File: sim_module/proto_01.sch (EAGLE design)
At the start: 4 parts, among them IC1 SIM900

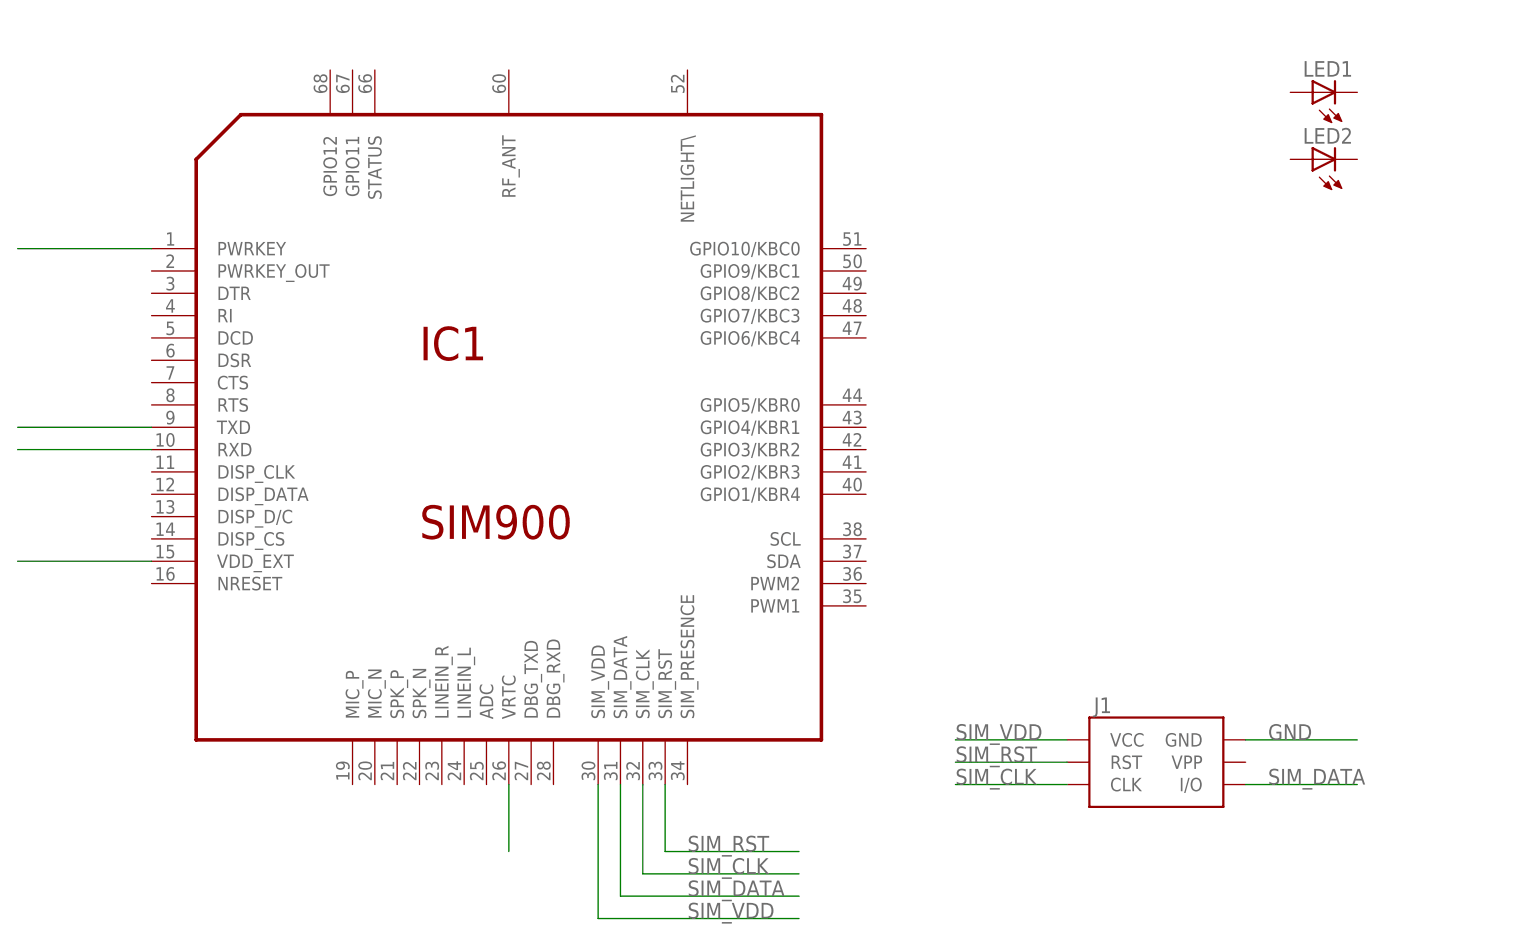
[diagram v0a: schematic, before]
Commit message: Connected leds to status and netlight pins in schematics
Connected leds to status and netlight pins in schematics
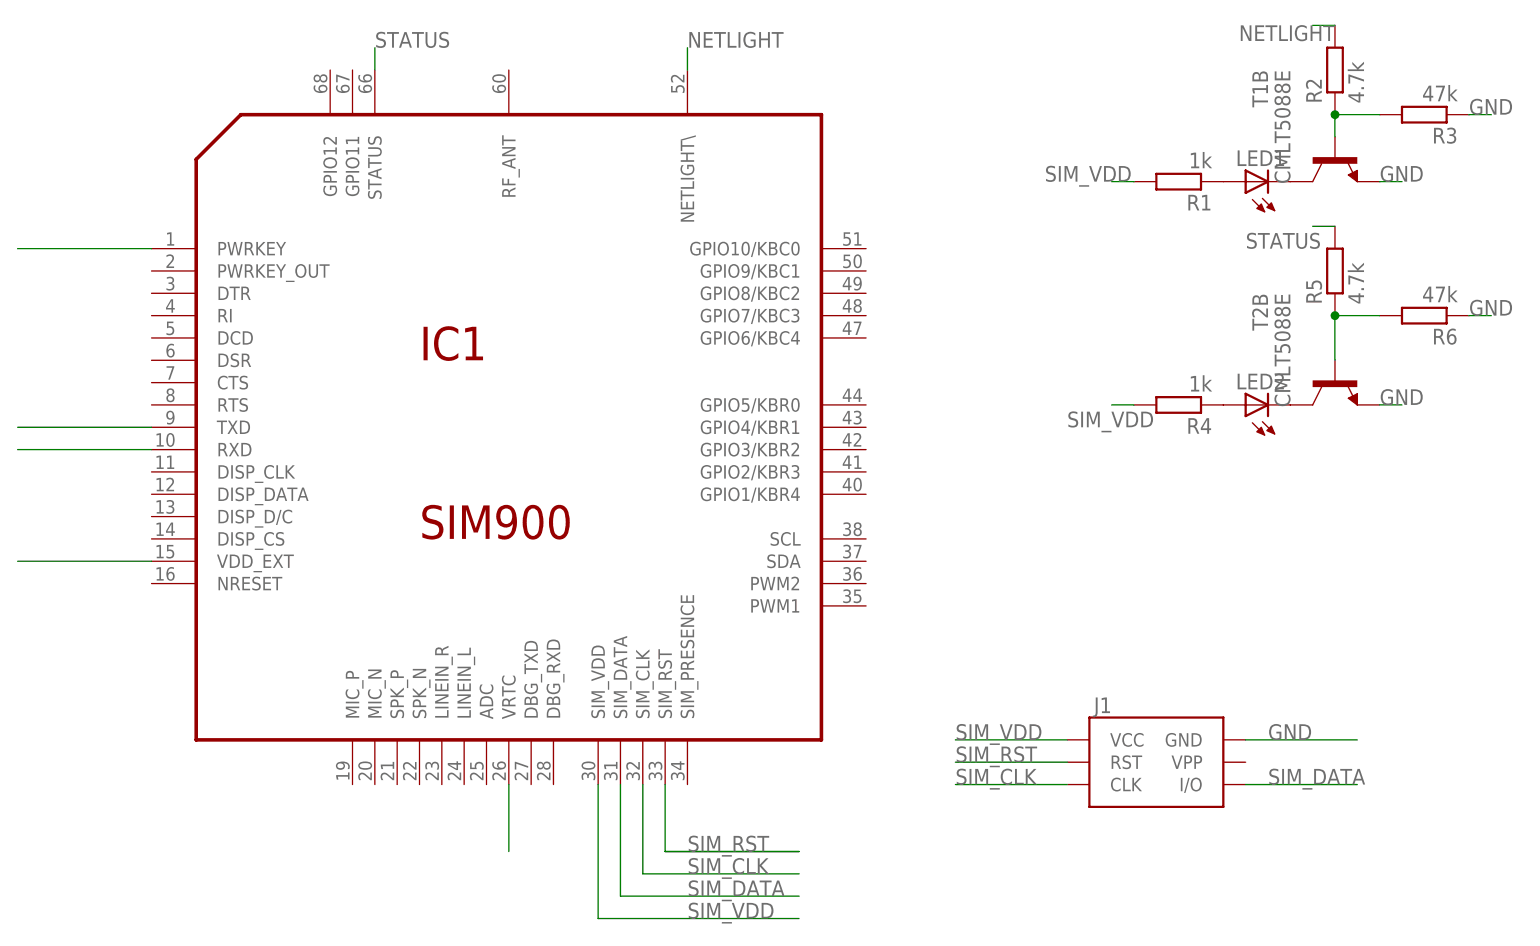
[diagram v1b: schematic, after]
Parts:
- added R1, R4: 1k, resistor:R-EU_R0805
- added R2, R5: 4.7k, resistor:R-EU_R0805
- added R3, R6: 47k, resistor:R-EU_R0805
- added T1, T2: CMLT5088E, transistor-neu-to92:CMLT5088E
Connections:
- new net N$10: LED2.A, R4.1
- new net N$11: R5.1, R6.2, T2B.B
- new net N$6: LED1.C, T1B.C
- new net N$7: LED1.A, R1.1
- new net N$8: R2.1, R3.2, T1B.B
- new net N$9: LED2.C, T2B.C
- new net NETLIGHT: IC1G$1.NETLIGHT\, R2.2
- new net STATUS: IC1G$1.STATUS, R5.2
- net GND: now also R3.1, R6.1, T1B.E, T2B.E
- net SIM_VDD: now also R1.2, R4.2
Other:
- moved on the sheet: LED1, LED2
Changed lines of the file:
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@@
 <?xml version="1.0" encoding="utf-8"?>
 <!DOCTYPE eagle SYSTEM "eagle.dtd">
-<eagle version="7.2.0">
+<eagle version="7.3.0">
 <drawing>
 <settings>
@@
 <part name="LED1" library="eagle-ltspice" deviceset="LED_E" device="SML0603"/>
 <part name="LED2" library="eagle-ltspice" deviceset="LED_E" device="SML0603"/>
+<part name="T1" library="transistor-neu-to92" deviceset="CMLT5088E" device=""/>
+<part name="T2" library="transistor-neu-to92" deviceset="CMLT5088E" device=""/>
+<part name="R1" library="resistor" deviceset="R-EU_" device="R0805" value="1k"/>
+<part name="R2" library="resistor" deviceset="R-EU_" device="R0805" value="4.7k"/>
+<part name="R3" library="resistor" deviceset="R-EU_" device="R0805" value="47k"/>
+<part name="R4" library="resistor" deviceset="R-EU_" device="R0805" value="1k"/>
+<part name="R5" library="resistor" deviceset="R-EU_" device="R0805" value="4.7k"/>
+<part name="R6" library="resistor" deviceset="R-EU_" device="R0805" value="47k"/>
 </parts>
 <sheets>
@@
 <instance part="J1" gate="J1" x="134.62" y="43.18"/>
 <instance part="IC1" gate="G$1" x="60.96" y="81.28"/>
-<instance part="LED1" gate="G$1" x="152.4" y="119.38" rot="R90"/>
-<instance part="LED2" gate="G$1" x="152.4" y="111.76" rot="R90"/>
+<instance part="LED1" gate="G$1" x="144.78" y="109.22" rot="R90"/>
+<instance part="LED2" gate="G$1" x="144.78" y="83.82" rot="R90"/>
+<instance part="T1" gate="B" x="154.94" y="111.76" rot="MR270"/>
+<instance part="T2" gate="B" x="154.94" y="86.36" rot="MR270"/>
+<instance part="R1" gate="G$1" x="137.16" y="109.22" rot="R180"/>
+<instance part="R2" gate="G$1" x="154.94" y="121.92" rot="R90"/>
+<instance part="R3" gate="G$1" x="165.1" y="116.84" rot="R180"/>
+<instance part="R4" gate="G$1" x="137.16" y="83.82" rot="R180"/>
+<instance part="R5" gate="G$1" x="154.94" y="99.06" rot="R90"/>
+<instance part="R6" gate="G$1" x="165.1" y="93.98" rot="R180"/>
 </instances>
 <busses>
@@
 <wire x1="78.74" y1="33.02" x2="93.98" y2="33.02" width="0.1524" layer="91"/>
 <label x="81.28" y="33.02" size="1.778" layer="95"/>
+<wire x1="78.74" y1="33.02" x2="93.98" y2="33.02" width="0.1524" layer="91"/>
 </segment>
 <segment>
@@
 <label x="111.76" y="45.72" size="1.778" layer="95"/>
 </segment>
+<segment>
+<pinref part="R1" gate="G$1" pin="2"/>
+<wire x1="132.08" y1="109.22" x2="129.54" y2="109.22" width="0.1524" layer="91"/>
+<label x="121.92" y="109.22" size="1.778" layer="95"/>
+</segment>
+<segment>
+<pinref part="R4" gate="G$1" pin="2"/>
+<wire x1="132.08" y1="83.82" x2="129.54" y2="83.82" width="0.1524" layer="91"/>
+<label x="124.46" y="81.28" size="1.778" layer="95"/>
+</segment>
 </net>
 <net name="GND" class="0">
@@
 <label x="147.32" y="45.72" size="1.778" layer="95"/>
 </segment>
+<segment>
+<pinref part="T1" gate="B" pin="E"/>
+<wire x1="160.02" y1="109.22" x2="162.56" y2="109.22" width="0.1524" layer="91"/>
+<label x="160.02" y="109.22" size="1.778" layer="95"/>
+</segment>
+<segment>
+<pinref part="R3" gate="G$1" pin="1"/>
+<wire x1="170.18" y1="116.84" x2="172.72" y2="116.84" width="0.1524" layer="91"/>
+<label x="170.18" y="116.84" size="1.778" layer="95"/>
+</segment>
+<segment>
+<pinref part="T2" gate="B" pin="E"/>
+<wire x1="160.02" y1="83.82" x2="162.56" y2="83.82" width="0.1524" layer="91"/>
+<label x="160.02" y="83.82" size="1.778" layer="95"/>
+</segment>
+<segment>
+<pinref part="R6" gate="G$1" pin="1"/>
+<wire x1="170.18" y1="93.98" x2="172.72" y2="93.98" width="0.1524" layer="91"/>
+<label x="170.18" y="93.98" size="1.778" layer="95"/>
+</segment>
 </net>
 <net name="N$1" class="0">
@@
 </segment>
 </net>
+<net name="N$6" class="0">
+<segment>
+<pinref part="LED1" gate="G$1" pin="C"/>
+<pinref part="T1" gate="B" pin="C"/>
+</segment>
+</net>
+<net name="N$7" class="0">
+<segment>
+<pinref part="R1" gate="G$1" pin="1"/>
+<pinref part="LED1" gate="G$1" pin="A"/>
+</segment>
+</net>
+<net name="N$8" class="0">
+<segment>
+<pinref part="T1" gate="B" pin="B"/>
+<pinref part="R2" gate="G$1" pin="1"/>
+<wire x1="154.94" y1="114.3" x2="154.94" y2="116.84" width="0.1524" layer="91"/>
+<pinref part="R3" gate="G$1" pin="2"/>
+<wire x1="160.02" y1="116.84" x2="154.94" y2="116.84" width="0.1524" layer="91"/>
+<junction x="154.94" y="116.84"/>
+</segment>
+</net>
+<net name="NETLIGHT" class="0">
+<segment>
+<pinref part="IC1" gate="G$1" pin="NETLIGHT\"/>
+<wire x1="81.28" y1="121.92" x2="81.28" y2="124.46" width="0.1524" layer="91"/>
+<label x="81.28" y="124.46" size="1.778" layer="95"/>
+</segment>
+<segment>
+<pinref part="R2" gate="G$1" pin="2"/>
+<wire x1="154.94" y1="127" x2="152.4" y2="127" width="0.1524" layer="91"/>
+<label x="154.94" y="127" size="1.778" layer="95" rot="R180"/>
+</segment>
+</net>
+<net name="N$9" class="0">
+<segment>
+<pinref part="T2" gate="B" pin="C"/>
+<pinref part="LED2" gate="G$1" pin="C"/>
+</segment>
+</net>
+<net name="N$10" class="0">
+<segment>
+<pinref part="R4" gate="G$1" pin="1"/>
+<pinref part="LED2" gate="G$1" pin="A"/>
+</segment>
+</net>
+<net name="N$11" class="0">
+<segment>
+<pinref part="T2" gate="B" pin="B"/>
+<pinref part="R5" gate="G$1" pin="1"/>
+<wire x1="154.94" y1="88.9" x2="154.94" y2="93.98" width="0.1524" layer="91"/>
+<pinref part="R6" gate="G$1" pin="2"/>
+<wire x1="160.02" y1="93.98" x2="154.94" y2="93.98" width="0.1524" layer="91"/>
+<junction x="154.94" y="93.98"/>
+</segment>
+</net>
+<net name="STATUS" class="0">
+<segment>
+<pinref part="IC1" gate="G$1" pin="STATUS"/>
+<wire x1="45.72" y1="121.92" x2="45.72" y2="124.46" width="0.1524" layer="91"/>
+<label x="45.72" y="124.46" size="1.778" layer="95"/>
+</segment>
+<segment>
+<pinref part="R5" gate="G$1" pin="2"/>
+<wire x1="154.94" y1="104.14" x2="152.4" y2="104.14" width="0.1524" layer="91"/>
+<label x="144.78" y="101.6" size="1.778" layer="95"/>
+</segment>
+</net>
